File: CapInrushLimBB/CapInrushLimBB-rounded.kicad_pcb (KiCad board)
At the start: 2 copper layers, 56.5 x 34.9 mm, 29 parts, among them J1 Screw_Terminal_01x02, J2 Screw_Terminal_01x02, K1 G5LE-1A, Q1 MPSA42, Q2 IRF9540N, Q3 MPSA42, Q4 Q_PMOS_GDSD

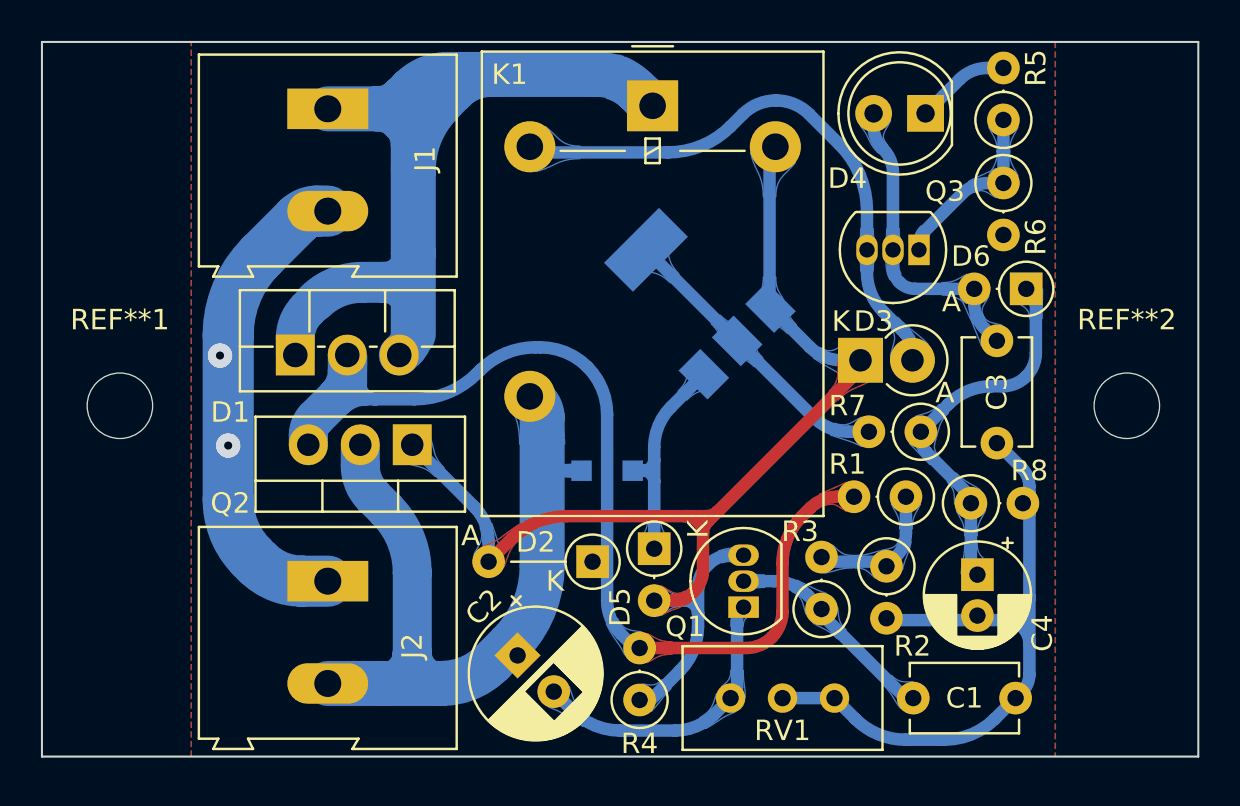
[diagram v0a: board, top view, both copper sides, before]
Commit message: Updated rounded tracks PCB and uploading modified TO-92 footprint (to increase clearance.)
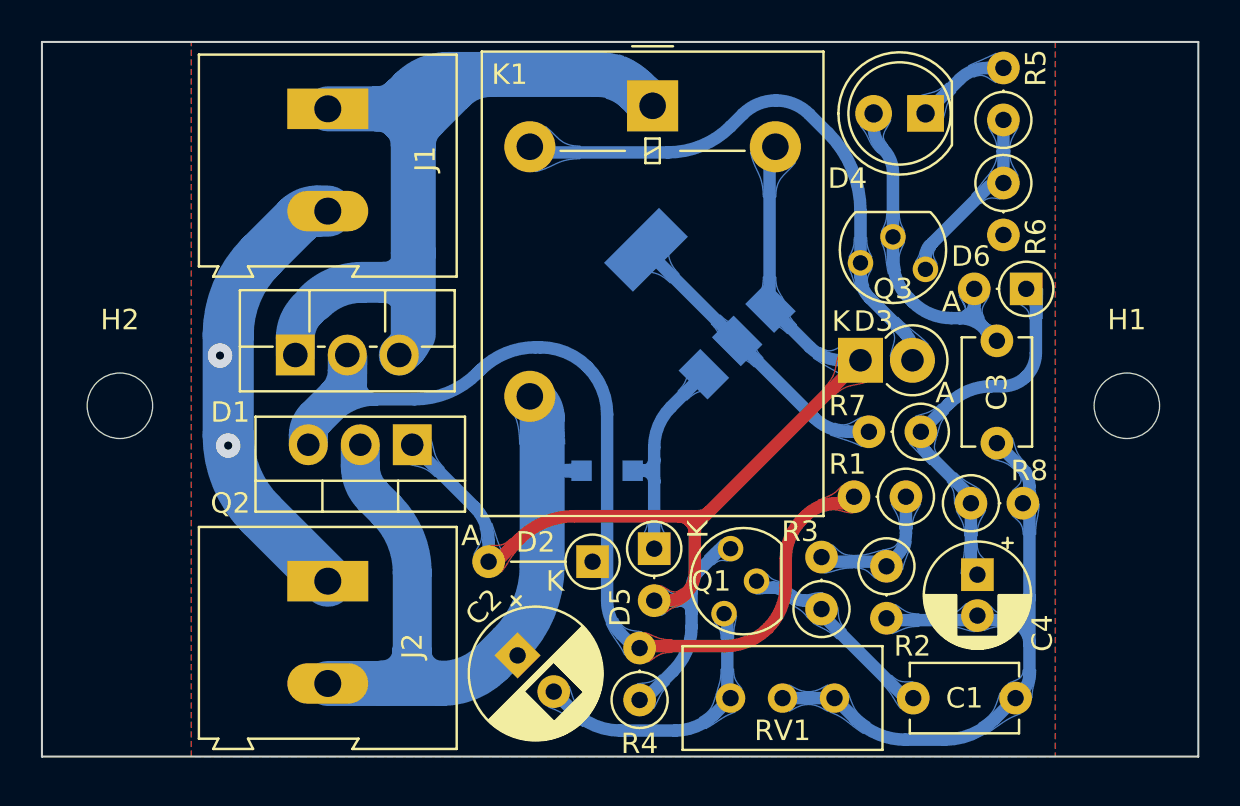
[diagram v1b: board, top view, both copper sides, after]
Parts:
- removed REF**1, REF**2: MountingHole_3.2mm_M3, MountingHole:MountingHole_3.2mm_M3
- added H1: MountingHole, MountingHole:MountingHole_3.2mm_M3, F.Cu at (260.0, 143.2)
- added H2: MountingHole, MountingHole:MountingHole_3.2mm_M3, F.Cu at (210.8, 143.2)
- Q1, Q3: footprint Package_TO_SOT_THT:TO-92_Inline -> CapInrushLim:TO-92_Inline
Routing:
- net /RL_Output: track 42.6 -> 38.2 mm
- net /RL_Input: track 54.8 -> 50.8 mm
- net Net-(C3-Pad2): track 15.2 -> 17.6 mm
- net /RLCoilHigh: track 65.5 -> 63.4 mm
- net /PolProtect: track 53.4 -> 55.1 mm
- net /Gnd: track 63.3 -> 61.9 mm
- net Net-(C1-Pad1): track 10.6 -> 9.50 mm
- net Net-(C2-Pad2): track 14.6 -> 14.0 mm
